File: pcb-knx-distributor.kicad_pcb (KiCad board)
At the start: 2 copper layers, 113.5 x 25.6 mm, 17 parts, among them J1 Conn_01x02_Pin, J10 Conn_01x02_Pin, J11 Conn_01x02_Pin, J12 Conn_01x02_Pin, J13 Conn_01x02_Pin, J14 Conn_01x02_Pin, J2 Conn_01x02_Pin, J3 Conn_01x02_Pin, J4 Conn_01x02_Pin, J5 Conn_01x02_Pin, J6 Conn_01x02_Pin, J7 Conn_01x02_Pin, J8 Conn_01x02_Pin, J9 Conn_01x02_Pin

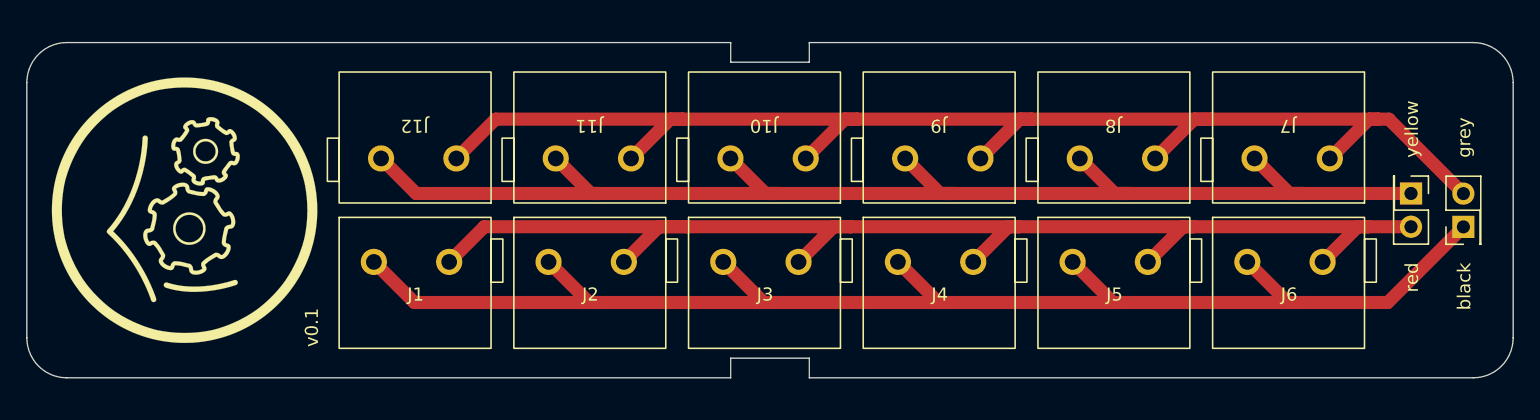
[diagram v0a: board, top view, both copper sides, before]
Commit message: Tracks on both sides
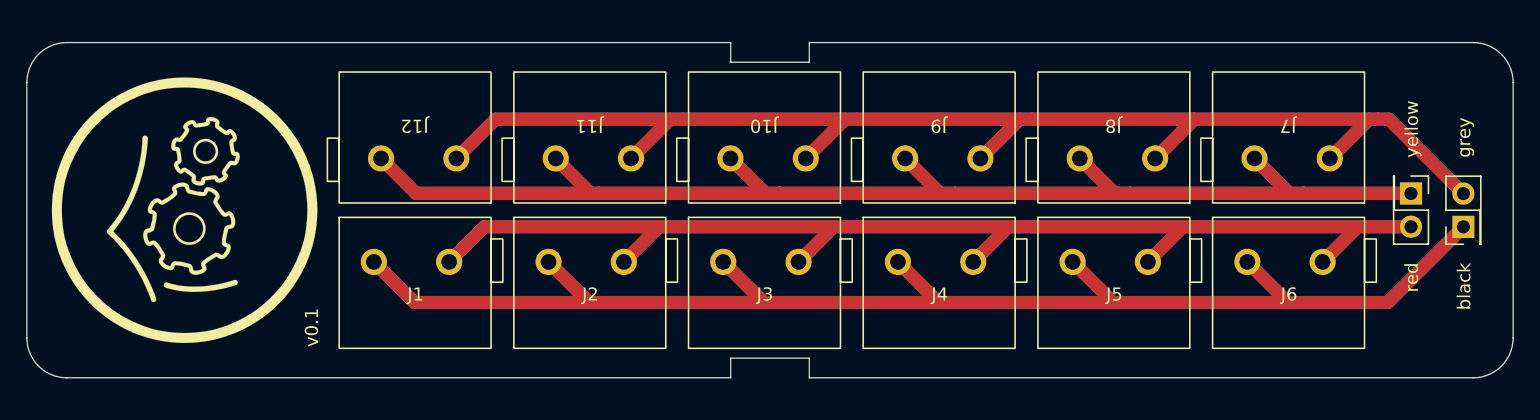
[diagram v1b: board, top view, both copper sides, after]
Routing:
- net /black: track 114.7 -> 217.6 mm
- net /grey: track 106.5 -> 203.4 mm
- net /yellow: track 103.8 -> 197.3 mm
- net /red: track 99.5 -> 187.1 mm
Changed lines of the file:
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@@
   (segment (start 48.75 67.95) (end 51.85 71.05) (width 1) (layer "F.Cu") (net 1))
   (segment (start 51.85 71.05) (end 66.55 71.05) (width 1) (layer "F.Cu") (net 1))
-  (segment (start 78.53 71.05) (end 79.75 71.05) (width 1) (layer "F.Cu") (net 1))
-  (segment (start 65.19 71.05) (end 66.55 71.05) (width 1) (layer "F.Cu") (net 1))
-  (segment (start 105.21 71.05) (end 106.35 71.05) (width 1) (layer "F.Cu") (net 1))
   (segment (start 79.75 71.05) (end 92.85 71.05) (width 1) (layer "F.Cu") (net 1))
-  (segment (start 91.87 71.05) (end 92.85 71.05) (width 1) (layer "F.Cu") (net 1))
   (segment (start 92.85 71.05) (end 106.35 71.05) (width 1) (layer "F.Cu") (net 1))
-  (segment (start 118.55 71.05) (end 119.8 71.05) (width 1) (layer "F.Cu") (net 1))
   (segment (start 88.77 67.95) (end 91.87 71.05) (width 1) (layer "F.Cu") (net 1))
   (segment (start 119.8 71.05) (end 126.175 71.05) (width 1) (layer "F.Cu") (net 1))
@@
   (segment (start 62.09 67.95) (end 65.19 71.05) (width 1) (layer "F.Cu") (net 1))
   (segment (start 106.35 71.05) (end 119.8 71.05) (width 1) (layer "F.Cu") (net 1))
+  (segment (start 92.8625 71.05) (end 106.3625 71.05) (width 1) (layer "B.Cu") (net 1))
+  (segment (start 66.5625 71.05) (end 79.7625 71.05) (width 1) (layer "B.Cu") (net 1))
+  (segment (start 88.7825 67.95) (end 91.8825 71.05) (width 1) (layer "B.Cu") (net 1))
+  (segment (start 51.8625 71.05) (end 66.5625 71.05) (width 1) (layer "B.Cu") (net 1))
+  (segment (start 102.1225 67.95) (end 105.2225 71.05) (width 1) (layer "B.Cu") (net 1))
+  (segment (start 75.4425 67.95) (end 78.5425 71.05) (width 1) (layer "B.Cu") (net 1))
+  (segment (start 126.1875 71.05) (end 131.9625 65.275) (width 1) (layer "B.Cu") (net 1))
+  (segment (start 79.7625 71.05) (end 92.8625 71.05) (width 1) (layer "B.Cu") (net 1))
+  (segment (start 62.1025 67.95) (end 65.2025 71.05) (width 1) (layer "B.Cu") (net 1))
+  (segment (start 115.4625 67.95) (end 118.5625 71.05) (width 1) (layer "B.Cu") (net 1))
+  (segment (start 48.7625 67.95) (end 51.8625 71.05) (width 1) (layer "B.Cu") (net 1))
+  (segment (start 119.8125 71.05) (end 126.1875 71.05) (width 1) (layer "B.Cu") (net 1))
+  (segment (start 106.3625 71.05) (end 119.8125 71.05) (width 1) (layer "B.Cu") (net 1))
   (segment (start 107.86 67.95) (end 110.545 65.265) (width 1) (layer "F.Cu") (net 2))
   (segment (start 111.35 65.265) (end 124.7 65.265) (width 1) (layer "F.Cu") (net 2))
   (segment (start 57.185 65.265) (end 72.75 65.265) (width 1) (layer "F.Cu") (net 2))
-  (segment (start 70.525 65.265) (end 72.75 65.265) (width 1) (layer "F.Cu") (net 2))
   (segment (start 54.5 67.95) (end 57.185 65.265) (width 1) (layer "F.Cu") (net 2))
   (segment (start 85.2 65.265) (end 98 65.265) (width 1) (layer "F.Cu") (net 2))
   (segment (start 72.75 65.265) (end 85.2 65.265) (width 1) (layer "F.Cu") (net 2))
-  (segment (start 123.885 65.265) (end 124.7 65.265) (width 1) (layer "F.Cu") (net 2))
-  (segment (start 83.865 65.265) (end 85.2 65.265) (width 1) (layer "F.Cu") (net 2))
   (segment (start 81.18 67.95) (end 83.865 65.265) (width 1) (layer "F.Cu") (net 2))
-  (segment (start 110.545 65.265) (end 111.35 65.265) (width 1) (layer "F.Cu") (net 2))
   (segment (start 121.2 67.95) (end 123.885 65.265) (width 1) (layer "F.Cu") (net 2))
   (segment (start 67.84 67.95) (end 70.525 65.265) (width 1) (layer "F.Cu") (net 2))
   (segment (start 124.7 65.265) (end 127.95 65.265) (width 1) (layer "F.Cu") (net 2))
   (segment (start 94.52 67.95) (end 97.205 65.265) (width 1) (layer "F.Cu") (net 2))
-  (segment (start 97.205 65.265) (end 98 65.265) (width 1) (layer "F.Cu") (net 2))
   (segment (start 98 65.265) (end 111.35 65.265) (width 1) (layer "F.Cu") (net 2))
+  (segment (start 54.5 67.95) (end 57.185 65.265) (width 1) (layer "B.Cu") (net 2))
+  (segment (start 72.75 65.265) (end 85.2 65.265) (width 1) (layer "B.Cu") (net 2))
+  (segment (start 67.84 67.95) (end 70.525 65.265) (width 1) (layer "B.Cu") (net 2))
+  (segment (start 98 65.265) (end 111.35 65.265) (width 1) (layer "B.Cu") (net 2))
+  (segment (start 81.18 67.95) (end 83.865 65.265) (width 1) (layer "B.Cu") (net 2))
+  (segment (start 107.86 67.95) (end 110.545 65.265) (width 1) (layer "B.Cu") (net 2))
+  (segment (start 85.2 65.265) (end 98 65.265) (width 1) (layer "B.Cu") (net 2))
+  (segment (start 111.35 65.265) (end 124.7 65.265) (width 1) (layer "B.Cu") (net 2))
+  (segment (start 57.185 65.265) (end 72.75 65.265) (width 1) (layer "B.Cu") (net 2))
+  (segment (start 94.52 67.95) (end 97.205 65.265) (width 1) (layer "B.Cu") (net 2))
+  (segment (start 124.7 65.265) (end 127.95 65.265) (width 1) (layer "B.Cu") (net 2))
+  (segment (start 121.2 67.95) (end 123.885 65.265) (width 1) (layer "B.Cu") (net 2))
   (segment (start 55.05 60.05) (end 58.05 57.05) (width 1) (layer "F.Cu") (net 3))
   (segment (start 81.73 60.05) (end 84.73 57.05) (width 1) (layer "F.Cu") (net 3))
   (segment (start 121.75 60.05) (end 124.75 57.05) (width 1) (layer "F.Cu") (net 3))
   (segment (start 112.7 57.05) (end 125.45 57.05) (width 1) (layer "F.Cu") (net 3))
-  (segment (start 71.39 57.05) (end 72.35 57.05) (width 1) (layer "F.Cu") (net 3))
-  (segment (start 124.75 57.05) (end 125.45 57.05) (width 1) (layer "F.Cu") (net 3))
-  (segment (start 84.73 57.05) (end 85.65 57.05) (width 1) (layer "F.Cu") (net 3))
   (segment (start 108.41 60.05) (end 111.41 57.05) (width 1) (layer "F.Cu") (net 3))
   (segment (start 72.35 57.05) (end 85.65 57.05) (width 1) (layer "F.Cu") (net 3))
@@
   (segment (start 126.265 57.05) (end 131.95 62.735) (width 1) (layer "F.Cu") (net 3))
   (segment (start 125.45 57.05) (end 126.265 57.05) (width 1) (layer "F.Cu") (net 3))
-  (segment (start 98.07 57.05) (end 99 57.05) (width 1) (layer "F.Cu") (net 3))
-  (segment (start 111.41 57.05) (end 112.7 57.05) (width 1) (layer "F.Cu") (net 3))
   (segment (start 58.05 57.05) (end 72.35 57.05) (width 1) (layer "F.Cu") (net 3))
+  (segment (start 55.06 60.05) (end 58.06 57.05) (width 1) (layer "B.Cu") (net 3))
+  (segment (start 72.36 57.05) (end 85.66 57.05) (width 1) (layer "B.Cu") (net 3))
+  (segment (start 108.42 60.05) (end 111.42 57.05) (width 1) (layer "B.Cu") (net 3))
+  (segment (start 99.01 57.05) (end 112.71 57.05) (width 1) (layer "B.Cu") (net 3))
+  (segment (start 112.71 57.05) (end 125.46 57.05) (width 1) (layer "B.Cu") (net 3))
+  (segment (start 68.4 60.05) (end 71.4 57.05) (width 1) (layer "B.Cu") (net 3))
+  (segment (start 121.76 60.05) (end 124.76 57.05) (width 1) (layer "B.Cu") (net 3))
+  (segment (start 85.66 57.05) (end 99.01 57.05) (width 1) (layer "B.Cu") (net 3))
+  (segment (start 58.06 57.05) (end 72.36 57.05) (width 1) (layer "B.Cu") (net 3))
+  (segment (start 125.46 57.05) (end 126.275 57.05) (width 1) (layer "B.Cu") (net 3))
+  (segment (start 126.275 57.05) (end 131.96 62.735) (width 1) (layer "B.Cu") (net 3))
+  (segment (start 95.08 60.05) (end 98.08 57.05) (width 1) (layer "B.Cu") (net 3))
+  (segment (start 81.74 60.05) (end 84.74 57.05) (width 1) (layer "B.Cu") (net 3))
   (segment (start 93.15 62.725) (end 106.5 62.725) (width 1) (layer "F.Cu") (net 4))
   (segment (start 65.95 62.725) (end 79.75 62.725) (width 1) (layer "F.Cu") (net 4))
-  (segment (start 78.655 62.725) (end 79.75 62.725) (width 1) (layer "F.Cu") (net 4))
-  (segment (start 91.995 62.725) (end 93.15 62.725) (width 1) (layer "F.Cu") (net 4))
   (segment (start 49.3 60.05) (end 51.975 62.725) (width 1) (layer "F.Cu") (net 4))
   (segment (start 119.75 62.725) (end 127.95 62.725) (width 1) (layer "F.Cu") (net 4))
-  (segment (start 105.335 62.725) (end 106.5 62.725) (width 1) (layer "F.Cu") (net 4))
   (segment (start 75.98 60.05) (end 78.655 62.725) (width 1) (layer "F.Cu") (net 4))
-  (segment (start 65.315 62.725) (end 65.95 62.725) (width 1) (layer "F.Cu") (net 4))
   (segment (start 116 60.05) (end 118.675 62.725) (width 1) (layer "F.Cu") (net 4))
   (segment (start 62.64 60.05) (end 65.315 62.725) (width 1) (layer "F.Cu") (net 4))
@@
   (segment (start 102.66 60.05) (end 105.335 62.725) (width 1) (layer "F.Cu") (net 4))
   (segment (start 79.75 62.725) (end 93.15 62.725) (width 1) (layer "F.Cu") (net 4))
-  (segment (start 118.675 62.725) (end 119.75 62.725) (width 1) (layer "F.Cu") (net 4))
   (segment (start 51.975 62.725) (end 65.95 62.725) (width 1) (layer "F.Cu") (net 4))
   (segment (start 106.5 62.725) (end 119.75 62.725) (width 1) (layer "F.Cu") (net 4))
+  (segment (start 102.635 60.025) (end 105.31 62.7) (width 1) (layer "B.Cu") (net 4))
+  (segment (start 119.725 62.7) (end 127.925 62.7) (width 1) (layer "B.Cu") (net 4))
+  (segment (start 65.925 62.7) (end 79.725 62.7) (width 1) (layer "B.Cu") (net 4))
+  (segment (start 89.295 60.025) (end 91.97 62.7) (width 1) (layer "B.Cu") (net 4))
+  (segment (start 51.95 62.7) (end 65.925 62.7) (width 1) (layer "B.Cu") (net 4))
+  (segment (start 62.615 60.025) (end 65.29 62.7) (width 1) (layer "B.Cu") (net 4))
+  (segment (start 79.725 62.7) (end 93.125 62.7) (width 1) (layer "B.Cu") (net 4))
+  (segment (start 49.275 60.025) (end 51.95 62.7) (width 1) (layer "B.Cu") (net 4))
+  (segment (start 93.125 62.7) (end 106.475 62.7) (width 1) (layer "B.Cu") (net 4))
+  (segment (start 115.975 60.025) (end 118.65 62.7) (width 1) (layer "B.Cu") (net 4))
+  (segment (start 106.475 62.7) (end 119.725 62.7) (width 1) (layer "B.Cu") (net 4))
+  (segment (start 75.955 60.025) (end 78.63 62.7) (width 1) (layer "B.Cu") (net 4))
 )

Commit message: Updated footprints
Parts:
- J1, J2, J3, J4, J5, J6: footprint haus-automatisierung:Wago-243-131 -> haus-automatisierung:Wago-243-211
- J10, J11, J12, J7, J8, J9: footprint haus-automatisierung:Wago-243-131 -> haus-automatisierung:Wago-243-212
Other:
- board text added: "v0.2"
- board text removed: "v0.1"
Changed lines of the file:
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@@
     (title "KNX Distributor")
     (date "2023-08-15")
-    (rev "0.1")
+    (rev "0.2")
     (company "haus-automatisierung.com")
     (comment 1 "Matthias Kleine")
@@
   (net 3 "/grey")
   (net 4 "/yellow")
-  (footprint "haus-automatisierung:Wago-243-131" (layer "F.Cu")
+  (footprint "haus-automatisierung:Wago-243-211" (layer "F.Cu")
     (at 112.8 64.55)
     (property "Sheetfile" "pcb-knx-distributor.kicad_sch")
@@
     )
   )
-  (footprint "haus-automatisierung:Wago-243-131" (layer "F.Cu")
+  (footprint "haus-automatisierung:Wago-243-211" (layer "F.Cu")
     (at 86.12 64.55)
     (property "Sheetfile" "pcb-knx-distributor.kicad_sch")
@@
       (stroke (width 0.01) (type solid)) (fill solid) (layer "F.SilkS"))
   )
-  (footprint "haus-automatisierung:Wago-243-131" (layer "F.Cu")
+  (footprint "haus-automatisierung:Wago-243-211" (layer "F.Cu")
     (at 59.44 64.55)
     (property "Sheetfile" "pcb-knx-distributor.kicad_sch")
@@
     )
   )
-  (footprint "haus-automatisierung:Wago-243-131" (layer "F.Cu")
+  (footprint "haus-automatisierung:Wago-243-212" (layer "F.Cu")
     (at 84.38 63.45 180)
     (property "Sheetfile" "pcb-knx-distributor.kicad_sch")
@@
     (pad "2" thru_hole circle (at 8.4 3.4 180) (size 2 2) (drill 1.2) (layers "*.Cu" "*.Mask")
       (net 4 "/yellow") (pinfunction "Pin_2") (pintype "passive"))
-    (model "/Users/matthiaskleine/Documents/KiCad/footprints/pcb-footprint-collection-kicad/haus-automatisierung.pretty/step/243-211.stp"
+    (model "/Users/matthiaskleine/Documents/KiCad/footprints/pcb-footprint-collection-kicad/haus-automatisierung.pretty/step/243-212.stp"
       (offset (xyz 0 0 0))
       (scale (xyz 1 1 1))
@@
     )
   )
-  (footprint "haus-automatisierung:Wago-243-131" (layer "F.Cu")
+  (footprint "haus-automatisierung:Wago-243-212" (layer "F.Cu")
     (at 124.4 63.45 180)
     (property "Sheetfile" "pcb-knx-distributor.kicad_sch")
@@
     (pad "2" thru_hole circle (at 8.4 3.4 180) (size 2 2) (drill 1.2) (layers "*.Cu" "*.Mask")
       (net 4 "/yellow") (pinfunction "Pin_2") (pintype "passive"))
-    (model "/Users/matthiaskleine/Documents/KiCad/footprints/pcb-footprint-collection-kicad/haus-automatisierung.pretty/step/243-211.stp"
+    (model "/Users/matthiaskleine/Documents/KiCad/footprints/pcb-footprint-collection-kicad/haus-automatisierung.pretty/step/243-212.stp"
       (offset (xyz 0 0 0))
       (scale (xyz 1 1 1))
@@
     )
   )
-  (footprint "haus-automatisierung:Wago-243-131" (layer "F.Cu")
+  (footprint "haus-automatisierung:Wago-243-212" (layer "F.Cu")
     (at 111.06 63.45 180)
     (property "Sheetfile" "pcb-knx-distributor.kicad_sch")
@@
     (pad "2" thru_hole circle (at 8.4 3.4 180) (size 2 2) (drill 1.2) (layers "*.Cu" "*.Mask")
       (net 4 "/yellow") (pinfunction "Pin_2") (pintype "passive"))
-    (model "/Users/matthiaskleine/Documents/KiCad/footprints/pcb-footprint-collection-kicad/haus-automatisierung.pretty/step/243-211.stp"
+    (model "/Users/matthiaskleine/Documents/KiCad/footprints/pcb-footprint-collection-kicad/haus-automatisierung.pretty/step/243-212.stp"
       (offset (xyz 0 0 0))
       (scale (xyz 1 1 1))
@@
     )
   )
-  (footprint "haus-automatisierung:Wago-243-131" (layer "F.Cu")
+  (footprint "haus-automatisierung:Wago-243-211" (layer "F.Cu")
     (at 99.46 64.55)
     (property "Sheetfile" "pcb-knx-distributor.kicad_sch")
@@
     )
   )
-  (footprint "haus-automatisierung:Wago-243-131" (layer "F.Cu")
+  (footprint "haus-automatisierung:Wago-243-212" (layer "F.Cu")
     (at 97.72 63.45 180)
     (property "Sheetfile" "pcb-knx-distributor.kicad_sch")
@@
     (pad "2" thru_hole circle (at 8.4 3.4 180) (size 2 2) (drill 1.2) (layers "*.Cu" "*.Mask")
       (net 4 "/yellow") (pinfunction "Pin_2") (pintype "passive"))
-    (model "/Users/matthiaskleine/Documents/KiCad/footprints/pcb-footprint-collection-kicad/haus-automatisierung.pretty/step/243-211.stp"
+    (model "/Users/matthiaskleine/Documents/KiCad/footprints/pcb-footprint-collection-kicad/haus-automatisierung.pretty/step/243-212.stp"
       (offset (xyz 0 0 0))
       (scale (xyz 1 1 1))
@@
     )
   )
-  (footprint "haus-automatisierung:Wago-243-131" (layer "F.Cu")
+  (footprint "haus-automatisierung:Wago-243-212" (layer "F.Cu")
     (at 71.04 63.45 180)
     (property "Sheetfile" "pcb-knx-distributor.kicad_sch")
@@
     (pad "2" thru_hole circle (at 8.4 3.4 180) (size 2 2) (drill 1.2) (layers "*.Cu" "*.Mask")
       (net 4 "/yellow") (pinfunction "Pin_2") (pintype "passive"))
-    (model "/Users/matthiaskleine/Documents/KiCad/footprints/pcb-footprint-collection-kicad/haus-automatisierung.pretty/step/243-211.stp"
+    (model "/Users/matthiaskleine/Documents/KiCad/footprints/pcb-footprint-collection-kicad/haus-automatisierung.pretty/step/243-212.stp"
       (offset (xyz 0 0 0))
       (scale (xyz 1 1 1))
@@
     )
   )
-  (footprint "haus-automatisierung:Wago-243-131" (layer "F.Cu")
+  (footprint "haus-automatisierung:Wago-243-211" (layer "F.Cu")
     (at 72.78 64.55)
     (property "Sheetfile" "pcb-knx-distributor.kicad_sch")
@@
     )
   )
-  (footprint "haus-automatisierung:Wago-243-131" (layer "F.Cu")
+  (footprint "haus-automatisierung:Wago-243-212" (layer "F.Cu")
     (at 57.7 63.45 180)
     (property "Sheetfile" "pcb-knx-distributor.kicad_sch")
@@
     (pad "2" thru_hole circle (at 8.4 3.4 180) (size 2 2) (drill 1.2) (layers "*.Cu" "*.Mask")
       (net 4 "/yellow") (pinfunction "Pin_2") (pintype "passive"))
-    (model "/Users/matthiaskleine/Documents/KiCad/footprints/pcb-footprint-collection-kicad/haus-automatisierung.pretty/step/243-211.stp"
+    (model "/Users/matthiaskleine/Documents/KiCad/footprints/pcb-footprint-collection-kicad/haus-automatisierung.pretty/step/243-212.stp"
       (offset (xyz 0 0 0))
       (scale (xyz 1 1 1))
@@
     )
   )
-  (footprint "haus-automatisierung:Wago-243-131" (layer "F.Cu")
+  (footprint "haus-automatisierung:Wago-243-211" (layer "F.Cu")
     (at 46.1 64.55)
     (property "Sheetfile" "pcb-knx-distributor.kicad_sch")
@@
     (effects (font (size 1 1) (thickness 0.15)) (justify left bottom))
   )
-  (gr_text "v0.1" (at 44.6 74.45 90) (layer "F.SilkS")
+  (gr_text "v0.2" (at 44.6 74.45 90) (layer "F.SilkS")
     (effects (font (size 1 1) (thickness 0.15)) (justify left bottom))
   )
